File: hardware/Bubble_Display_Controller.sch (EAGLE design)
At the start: 37 parts, among them J1 ICSP, Q1 BSS84, Q10 IRFML8244, Q11 IRFML8244, Q12 IRFML8244, Q13 IRFML8244, Q14 IRFML8244, Q15 IRFML8244, Q16 IRFML8244, Q2 BSS84, Q3 BSS84, Q4 BSS84, Q5 BSS84, Q6 BSS84, Q7 BSS84, Q8 BSS84, Q9 IRFML8244, U4 ATMEGA328, Y1 16MHz

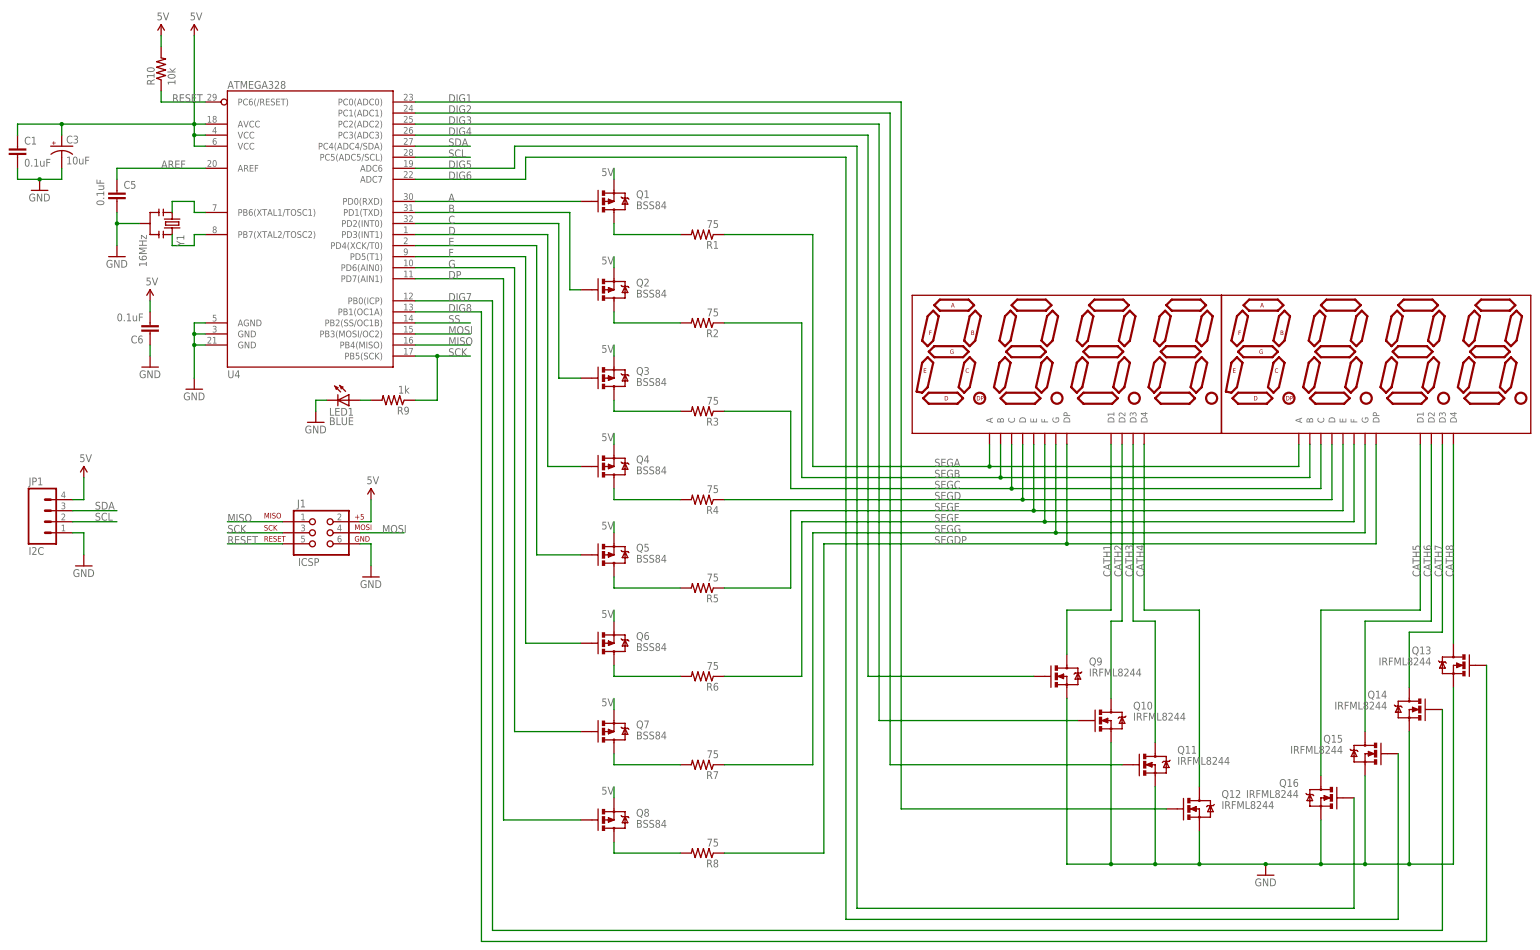
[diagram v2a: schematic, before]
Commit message: Some signal name changes
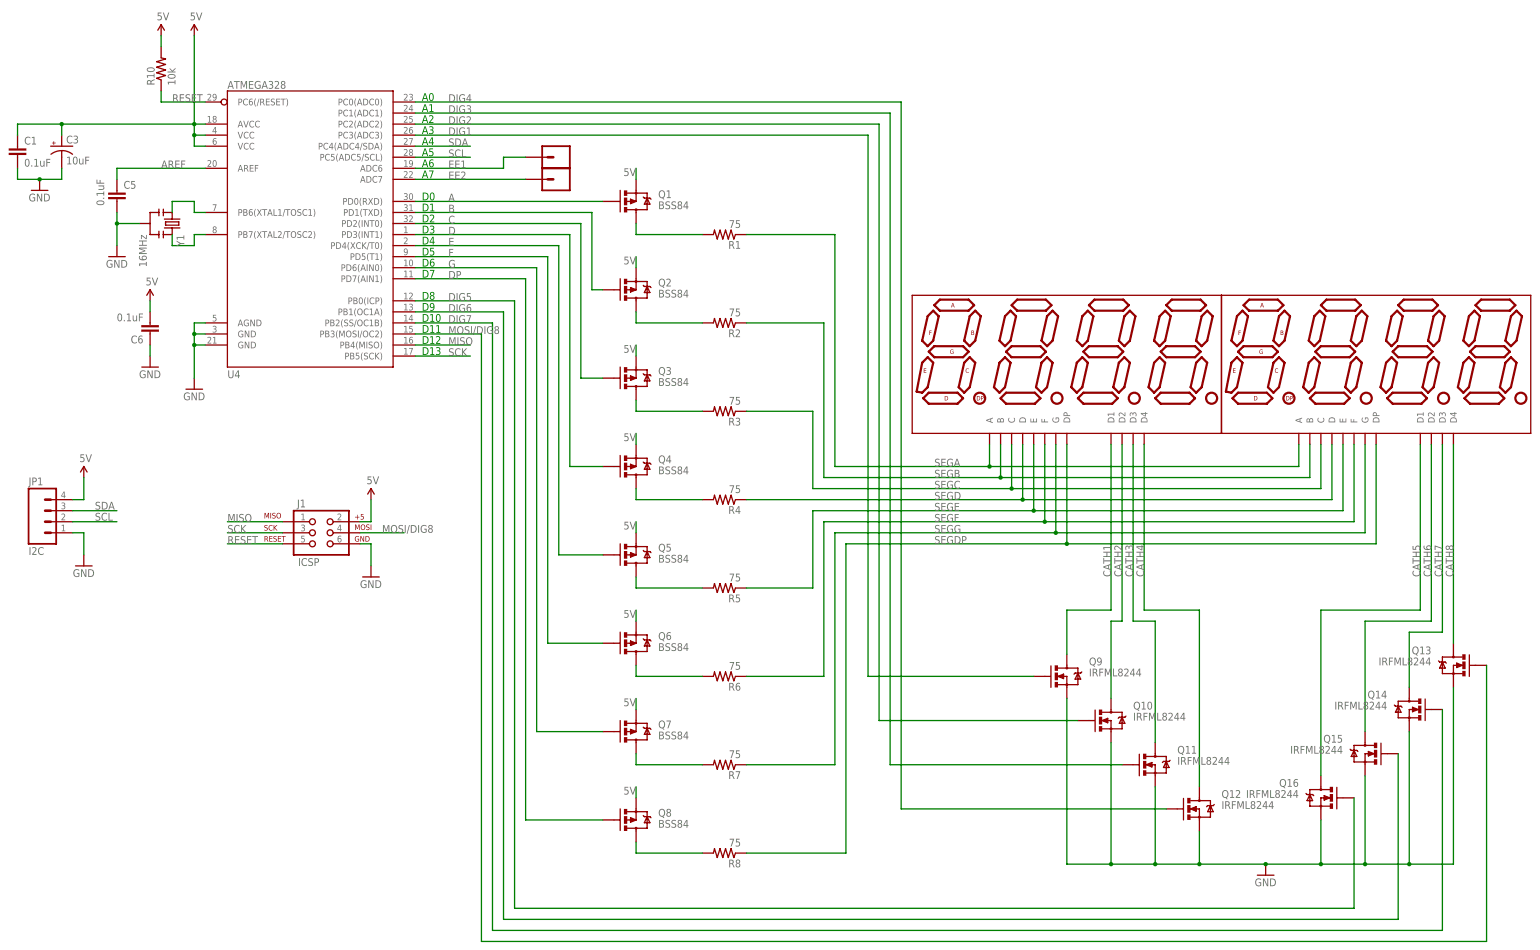
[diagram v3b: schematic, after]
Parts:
- removed LED1: BLUE, ChipsParts:LED-0805
- removed R9: 1k, SparkFun-Resistors:RESISTOR0805-RES
- added JP2, JP3: BREADBD_VIA, ChipsParts:BREADBD_VIA
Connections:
- removed net DIG8: Q13.G, U4.PB1(OC1A)
- removed net MOSI: J1.4, U4.PB3(MOSI/OC2)
- removed net N$2: LED1.A, R9.2
- removed net SS: U4.PB2(SS/OC1B)
- new net EE1: JP2.1, U4.ADC6
- new net EE2: JP3.1, U4.ADC7
- new net MOSI/DIG8: J1.4, Q13.G, U4.PB3(MOSI/OC2)
- net DIG1: now also Q9.G, U4.PC3(ADC3); no longer Q12.G, U4.PC0(ADC0)
- net DIG2: now also Q10.G, U4.PC2(ADC2); no longer Q11.G, U4.PC1(ADC1)
- net DIG3: now also Q11.G, U4.PC1(ADC1); no longer Q10.G, U4.PC2(ADC2)
- net DIG4: now also Q12.G, U4.PC0(ADC0); no longer Q9.G, U4.PC3(ADC3)
- net DIG5: now also U4.PB0(ICP); no longer U4.ADC6
- net DIG6: now also U4.PB1(OC1A); no longer U4.ADC7
- net DIG7: now also U4.PB2(SS/OC1B); no longer U4.PB0(ICP)
- net GND: no longer LED1.C
- net SCK: no longer R9.1
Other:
- note added: "A0"
- note added: "A1"
- note added: "A2"
- note added: "A3"
- note added: "A4"
- note added: "A5"
- note added: "A6"
- note added: "A7"
- note added: "D0"
- note added: "D1"
- note added: "D10"
- note added: "D11"
- note added: "D12"
- note added: "D13"
- note added: "D2"
- note added: "D3"
- note added: "D4"
- note added: "D5"
- note added: "D6"
- note added: "D7"
- note added: "D8"
- note added: "D9"
- moved on the sheet: Q1, Q2, Q3, Q4, Q5, Q6, Q7, Q8, R1, R2, R3, R4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

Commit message: New HW version started. Bringing FW forward.
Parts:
- removed Q1, Q2, Q3, Q4, Q5, Q6, Q7, Q8: BSS84, SparkFun-DiscreteSemi:MOSFET-PCHANNELSMD
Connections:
- removed net N$23: Q5.D, R5.2
- removed net N$25: Q1.D, R1.2
- removed net N$27: Q6.D, R6.2
- removed net N$28: Q2.D, R2.2
- removed net N$30: Q3.D, R3.2
- removed net N$32: Q4.D, R4.2
- removed net N$33: Q7.D, R7.2
- removed net N$34: Q8.D, R8.2
- net 5V: no longer Q1.S, Q2.S, Q3.S, Q4.S, Q5.S, Q6.S, Q7.S, Q8.S
- net A: now also R1.2; no longer Q1.G
- net B: now also R2.2; no longer Q2.G
- net C: now also R3.2; no longer Q3.G
- net D: now also R4.2; no longer Q4.G
- net DP: now also R8.2; no longer Q8.G
- net E: now also R5.2; no longer Q5.G
- net F: now also R6.2; no longer Q6.G
- net G: now also R7.2; no longer Q7.G
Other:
- moved on the sheet: Q10, Q11, Q12, Q13, Q14, Q15, Q16, Q9, R1, R2, R3, R4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

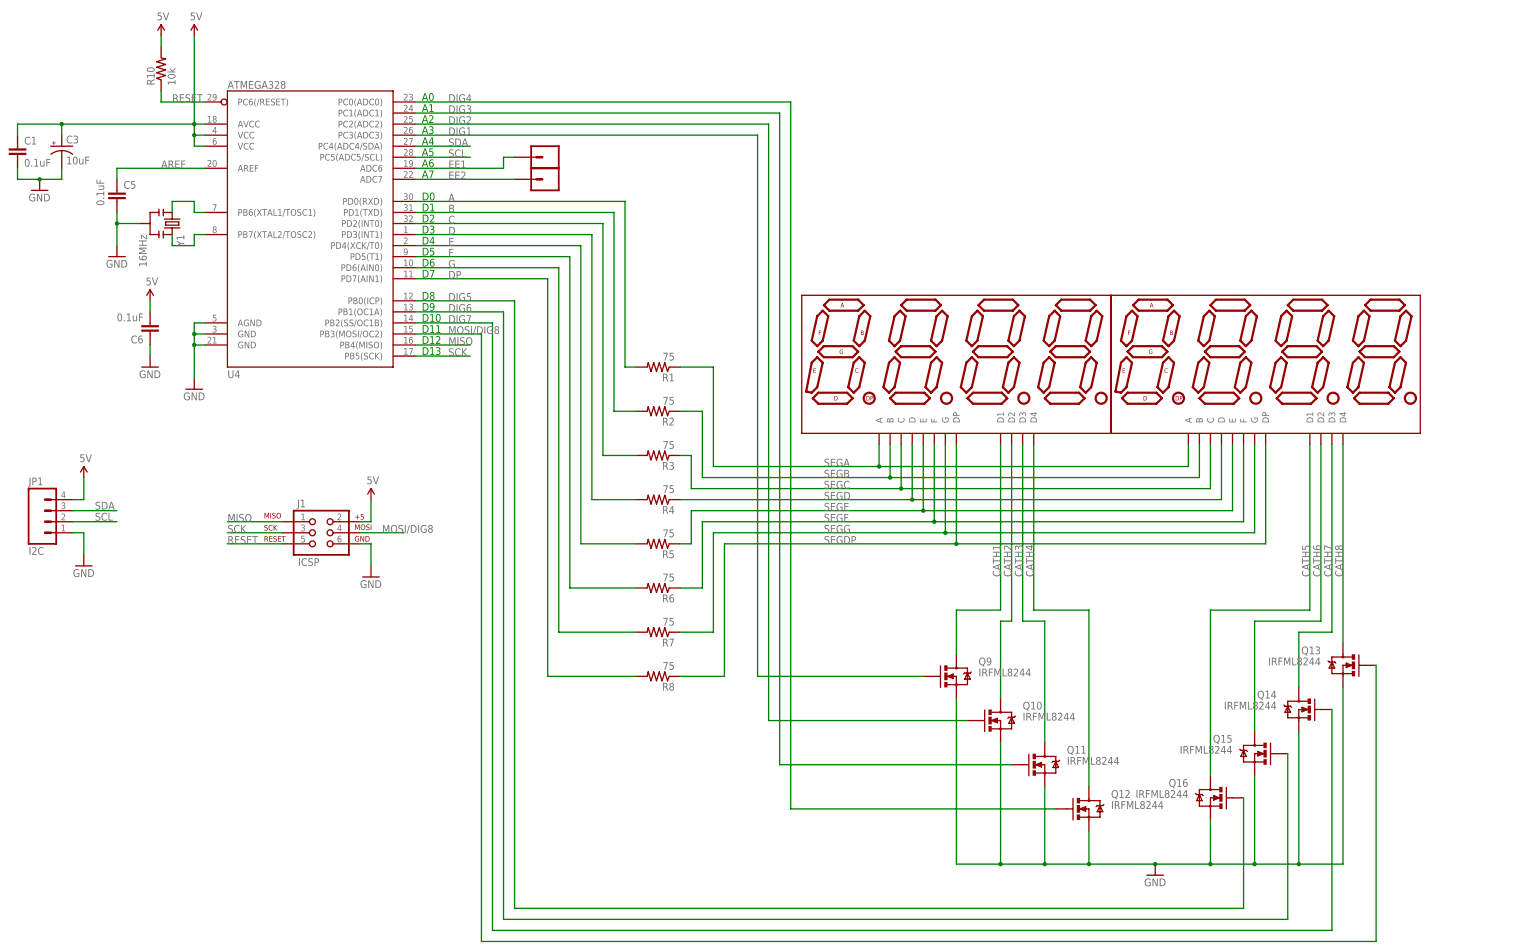
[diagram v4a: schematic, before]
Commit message: Ordered new board, 8Jyd7Mea. Updating docs to match.
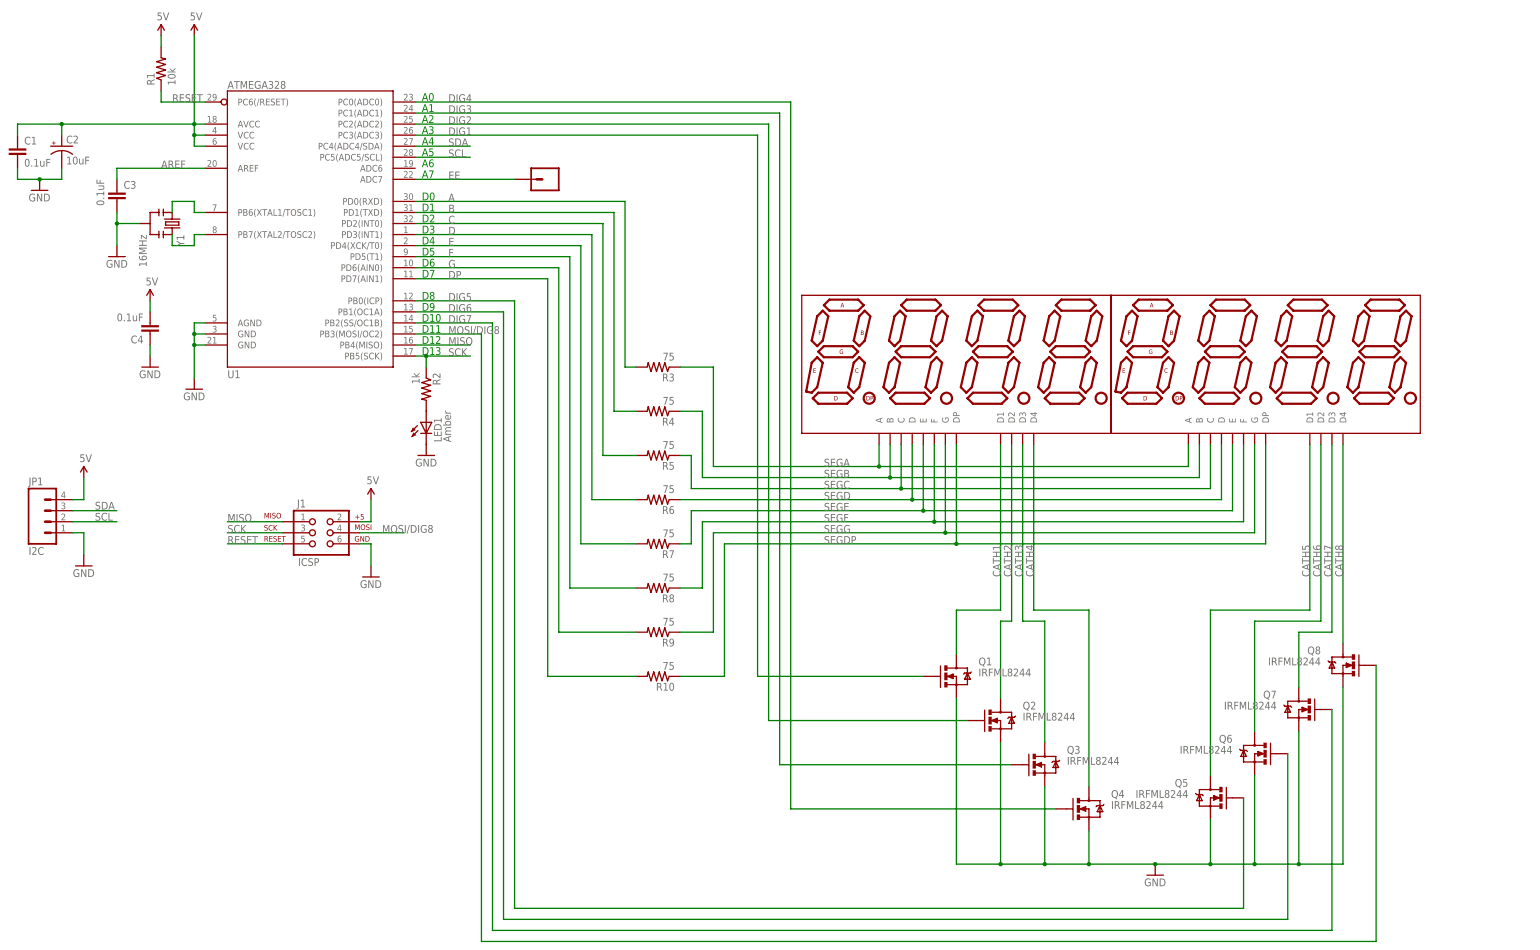
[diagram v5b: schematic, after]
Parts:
- removed C5: 0.1uF, SparkFun-Capacitors:CAP0805
- removed JP3: BREADBD_VIA, ChipsParts:BREADBD_VIA
- added C2: 10uF, ChipsParts:CAP_POL0805
- added LED1: Amber, ChipsParts:LED-0805
- added R9: 75, SparkFun-Resistors:RESISTOR0805-RES
- C3: value 10uF -> 0.1uF; device ChipsParts:CAP_POL0805 -> SparkFun-Capacitors:CAP0805
- R1: value 75 -> 10k
- R10: value 10k -> 75
- R2: value 75 -> 1k
- renumbered C6 to C4, Q10 to Q2, Q11 to Q3, Q12 to Q4, Q13 to Q8, Q14 to Q7, Q15 to Q6, Q16 to Q5, Q9 to Q1, U4 to U1
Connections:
- removed net EE1: JP2.1, U1.ADC6
- removed net EE2: JP3.1, U1.ADC7
- new net EE: JP2.1, U1.ADC7
- new net N$1: LED1.A, R2.2
- net 5V: now also C2.+, R1.2; no longer C3.+, R10.2
- net A: now also R3.2; no longer R1.2
- net AREF: now also C3.1; no longer C5.1
- net B: now also R4.2; no longer R2.2
- net C: now also R5.2; no longer R3.2
- net D: now also R6.2; no longer R4.2
- net DP: now also R10.2; no longer R8.2
- net E: now also R7.2; no longer R5.2
- net F: now also R8.2; no longer R6.2
- net G: now also R9.2; no longer R7.2
- net GND: now also C2.-, C3.2, LED1.C; no longer C3.-, C5.2
- net RESET: now also R1.1; no longer R10.1
- net SCK: now also R2.1
- net SEGA: now also R3.1; no longer R1.1
- net SEGB: now also R4.1; no longer R2.1
- net SEGC: now also R5.1; no longer R3.1
- net SEGD: now also R6.1; no longer R4.1
- net SEGDP: now also R10.1; no longer R8.1
- net SEGE: now also R7.1; no longer R5.1
- net SEGF: now also R8.1; no longer R6.1
- net SEGG: now also R9.1; no longer R7.1
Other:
- moved on the sheet: R1, R10, R2, R3, R4, R5, R6, R7, R8
